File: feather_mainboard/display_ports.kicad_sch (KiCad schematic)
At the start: 1 part, among them J1 61300811121

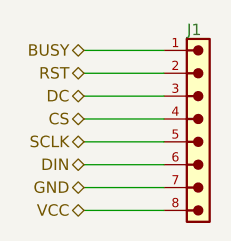
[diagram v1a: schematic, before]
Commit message: changed footprints location to match the new folder. TODO: check if the path is working on another computer
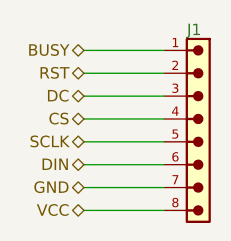
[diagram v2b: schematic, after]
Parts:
- J1: footprint footprints:61300811121 -> Custom footprints:61300811121
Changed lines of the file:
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@@
 			)
 		)
-		(property "Footprint" "footprints:61300811121"
+		(property "Footprint" "Custom footprints:61300811121"
 			(at 153.67 90.17 0)
 			(effects
